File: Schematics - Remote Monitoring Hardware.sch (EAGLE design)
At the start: 49 parts, among them IC1 MSP430G2 Socket, IC2 TPS77301, IC3 Xbee S3 Socket, IC4 MAX31855T, J7 53047-06, Q1 MC-405

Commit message: board and schematics update May 25 2017
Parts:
- removed J5: (no value), SparkFun-Connectors:CONN_023.5MM
- added J5A: (no value), SparkFun-Connectors:CONN_023.5MM
- added J5B: PCC-SMP, custom parts:PCC-SMP
- C7: value 1uF/6.3V -> 10uF
- C8: value 100uF -> 100nF
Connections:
- removed net DIN: J6.2
- removed net DOUT: J6.3
- net N$14: now also J5A.2, J5B.T-; no longer J5.2
- net N$15: now also J5A.1, J5B.T+; no longer J5.1
- net P1.1: now also J6.3
- net P1.2: now also J6.2
- net VCC: now also S2.1; no longer S2.2
- net VCC_XBEE: now also S2.2; no longer S2.1
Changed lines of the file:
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@@
 <classes>
 <class number="0" name="default" width="0.2032" drill="0">
+<clearance class="0" value="0.205"/>
 </class>
 <class number="1" name="vcc" width="0.3048" drill="0">
@@
 <part name="C6" library="eagle-ltspice" deviceset="C" device="" value="100nF"/>
 <part name="IC2" library="texas" deviceset="TPS773*" device="" technology="01"/>
-<part name="C7" library="eagle-ltspice" deviceset="C" device="" value="1uF/6.3V"/>
+<part name="C7" library="eagle-ltspice" deviceset="C" device="" value="10uF"/>
 <part name="GND7" library="supply1" deviceset="GND" device=""/>
 <part name="R5" library="eagle-ltspice" deviceset="R" device="" value="53.8k"/>
@@
 <part name="GND9" library="supply1" deviceset="GND" device=""/>
 <part name="R7" library="eagle-ltspice" deviceset="R" device="" value="250k"/>
-<part name="C8" library="eagle-ltspice" deviceset="C" device="" value="100uF"/>
+<part name="C8" library="eagle-ltspice" deviceset="C" device="" value="100nF"/>
 <part name="GND10" library="supply1" deviceset="GND" device=""/>
 <part name="GND11" library="supply1" deviceset="GND" device=""/>
@@
 <part name="J4" library="SparkFun-Connectors" deviceset="CONN_02" device="3.5MM"/>
 <part name="Q1" library="crystal" deviceset="MC-405" device=""/>
-<part name="J5" library="SparkFun-Connectors" deviceset="CONN_02" device="3.5MM"/>
+<part name="J5A" library="SparkFun-Connectors" deviceset="CONN_02" device="3.5MM"/>
+<part name="J5B" library="custom parts" deviceset="PCC-SMP" device=""/>
 </parts>
 <sheets>
@@
 </instance>
 <instance part="Q1" gate="P" x="38.1" y="55.88" rot="R90"/>
-<instance part="J5" gate="G$1" x="27.94" y="109.22" smashed="yes">
-<attribute name="VALUE" x="22.86" y="104.394" size="1.778" layer="96" font="vector"/>
-<attribute name="NAME" x="25.4" y="114.808" size="1.778" layer="95" font="vector"/>
+<instance part="J5A" gate="G$1" x="27.94" y="114.3" smashed="yes">
+<attribute name="VALUE" x="22.86" y="109.474" size="1.778" layer="96" font="vector"/>
+<attribute name="NAME" x="25.4" y="119.888" size="1.778" layer="95" font="vector"/>
 </instance>
+<instance part="J5B" gate="G$1" x="25.4" y="106.68"/>
 </instances>
 <busses>
@@
 <label x="228.6" y="58.42" size="1.778" layer="95"/>
 <pinref part="J7" gate="-5" pin="S"/>
-</segment>
-<segment>
-<pinref part="S2" gate="G$1" pin="2"/>
-<wire x1="187.96" y1="198.12" x2="195.58" y2="198.12" width="0.1524" layer="91"/>
-<label x="193.04" y="198.12" size="1.778" layer="95"/>
 </segment>
 <segment>
@@
 <label x="63.5" y="134.62" size="1.778" layer="95"/>
 </segment>
+<segment>
+<pinref part="S2" gate="G$1" pin="1"/>
+<wire x1="187.96" y1="195.58" x2="195.58" y2="195.58" width="0.1524" layer="91"/>
+<label x="193.04" y="195.58" size="1.778" layer="95"/>
+</segment>
 </net>
 <net name="P1.0" class="0">
@@
 <label x="228.6" y="48.26" size="1.778" layer="95"/>
 <pinref part="J7" gate="-1" pin="S"/>
+</segment>
+<segment>
+<pinref part="J6" gate="1" pin="2"/>
+<wire x1="185.42" y1="53.34" x2="195.58" y2="53.34" width="0.1524" layer="91"/>
+<label x="190.5" y="53.34" size="1.778" layer="95"/>
 </segment>
 </net>
@@
 <label x="228.6" y="60.96" size="1.778" layer="95"/>
 <pinref part="J7" gate="-6" pin="S"/>
+</segment>
+<segment>
+<pinref part="J6" gate="1" pin="3"/>
+<wire x1="185.42" y1="55.88" x2="195.58" y2="55.88" width="0.1524" layer="91"/>
+<label x="190.5" y="55.88" size="1.778" layer="95"/>
 </segment>
 </net>
@@
 <net name="N$14" class="0">
 <segment>
-<wire x1="38.1" y1="111.76" x2="38.1" y2="116.84" width="0.1524" layer="91"/>
 <pinref part="L1" gate="G$1" pin="2"/>
+<wire x1="35.56" y1="116.84" x2="38.1" y2="116.84" width="0.1524" layer="91"/>
+<pinref part="J5A" gate="G$1" pin="2"/>
 <wire x1="38.1" y1="116.84" x2="43.18" y2="116.84" width="0.1524" layer="91"/>
-<wire x1="38.1" y1="111.76" x2="35.56" y2="111.76" width="0.1524" layer="91"/>
-<pinref part="J5" gate="G$1" pin="2"/>
+<wire x1="33.02" y1="109.22" x2="38.1" y2="109.22" width="0.1524" layer="91"/>
+<wire x1="38.1" y1="109.22" x2="38.1" y2="116.84" width="0.1524" layer="91"/>
+<junction x="38.1" y="116.84"/>
+<pinref part="J5B" gate="G$1" pin="T-"/>
 </segment>
 </net>
 <net name="N$15" class="0">
 <segment>
-<wire x1="38.1" y1="109.22" x2="38.1" y2="104.14" width="0.1524" layer="91"/>
 <pinref part="L2" gate="G$1" pin="1"/>
-<wire x1="38.1" y1="104.14" x2="43.18" y2="104.14" width="0.1524" layer="91"/>
-<wire x1="35.56" y1="109.22" x2="38.1" y2="109.22" width="0.1524" layer="91"/>
-<pinref part="J5" gate="G$1" pin="1"/>
+<pinref part="J5A" gate="G$1" pin="1"/>
+<wire x1="40.64" y1="104.14" x2="43.18" y2="104.14" width="0.1524" layer="91"/>
+<wire x1="35.56" y1="114.3" x2="40.64" y2="114.3" width="0.1524" layer="91"/>
+<wire x1="40.64" y1="114.3" x2="40.64" y2="104.14" width="0.1524" layer="91"/>
+<junction x="40.64" y="104.14"/>
+<wire x1="33.02" y1="104.14" x2="40.64" y2="104.14" width="0.1524" layer="91"/>
+<pinref part="J5B" gate="G$1" pin="T+"/>
 </segment>
 </net>
@@
 </segment>
 <segment>
-<pinref part="S2" gate="G$1" pin="1"/>
-<wire x1="187.96" y1="195.58" x2="195.58" y2="195.58" width="0.1524" layer="91"/>
-<label x="193.04" y="195.58" size="1.778" layer="95"/>
-</segment>
-<segment>
 <wire x1="218.44" y1="109.22" x2="218.44" y2="106.68" width="0.1524" layer="91"/>
 <pinref part="R14" gate="G$1" pin="2"/>
@@
 <label x="190.5" y="50.8" size="1.778" layer="95"/>
 </segment>
+<segment>
+<pinref part="S2" gate="G$1" pin="2"/>
+<wire x1="187.96" y1="198.12" x2="195.58" y2="198.12" width="0.1524" layer="91"/>
+<label x="193.04" y="198.12" size="1.778" layer="95"/>
+</segment>
 </net>
 <net name="N$17" class="0">
@@
 </segment>
 </net>
-<net name="DOUT" class="0">
-<segment>
-<pinref part="J6" gate="1" pin="3"/>
-<wire x1="185.42" y1="55.88" x2="195.58" y2="55.88" width="0.1524" layer="91"/>
-<label x="190.5" y="55.88" size="1.778" layer="95"/>
-</segment>
-</net>
-<net name="DIN" class="0">
-<segment>
-<pinref part="J6" gate="1" pin="2"/>
-<wire x1="185.42" y1="53.34" x2="195.58" y2="53.34" width="0.1524" layer="91"/>
-<label x="190.5" y="53.34" size="1.778" layer="95"/>
-</segment>
-</net>

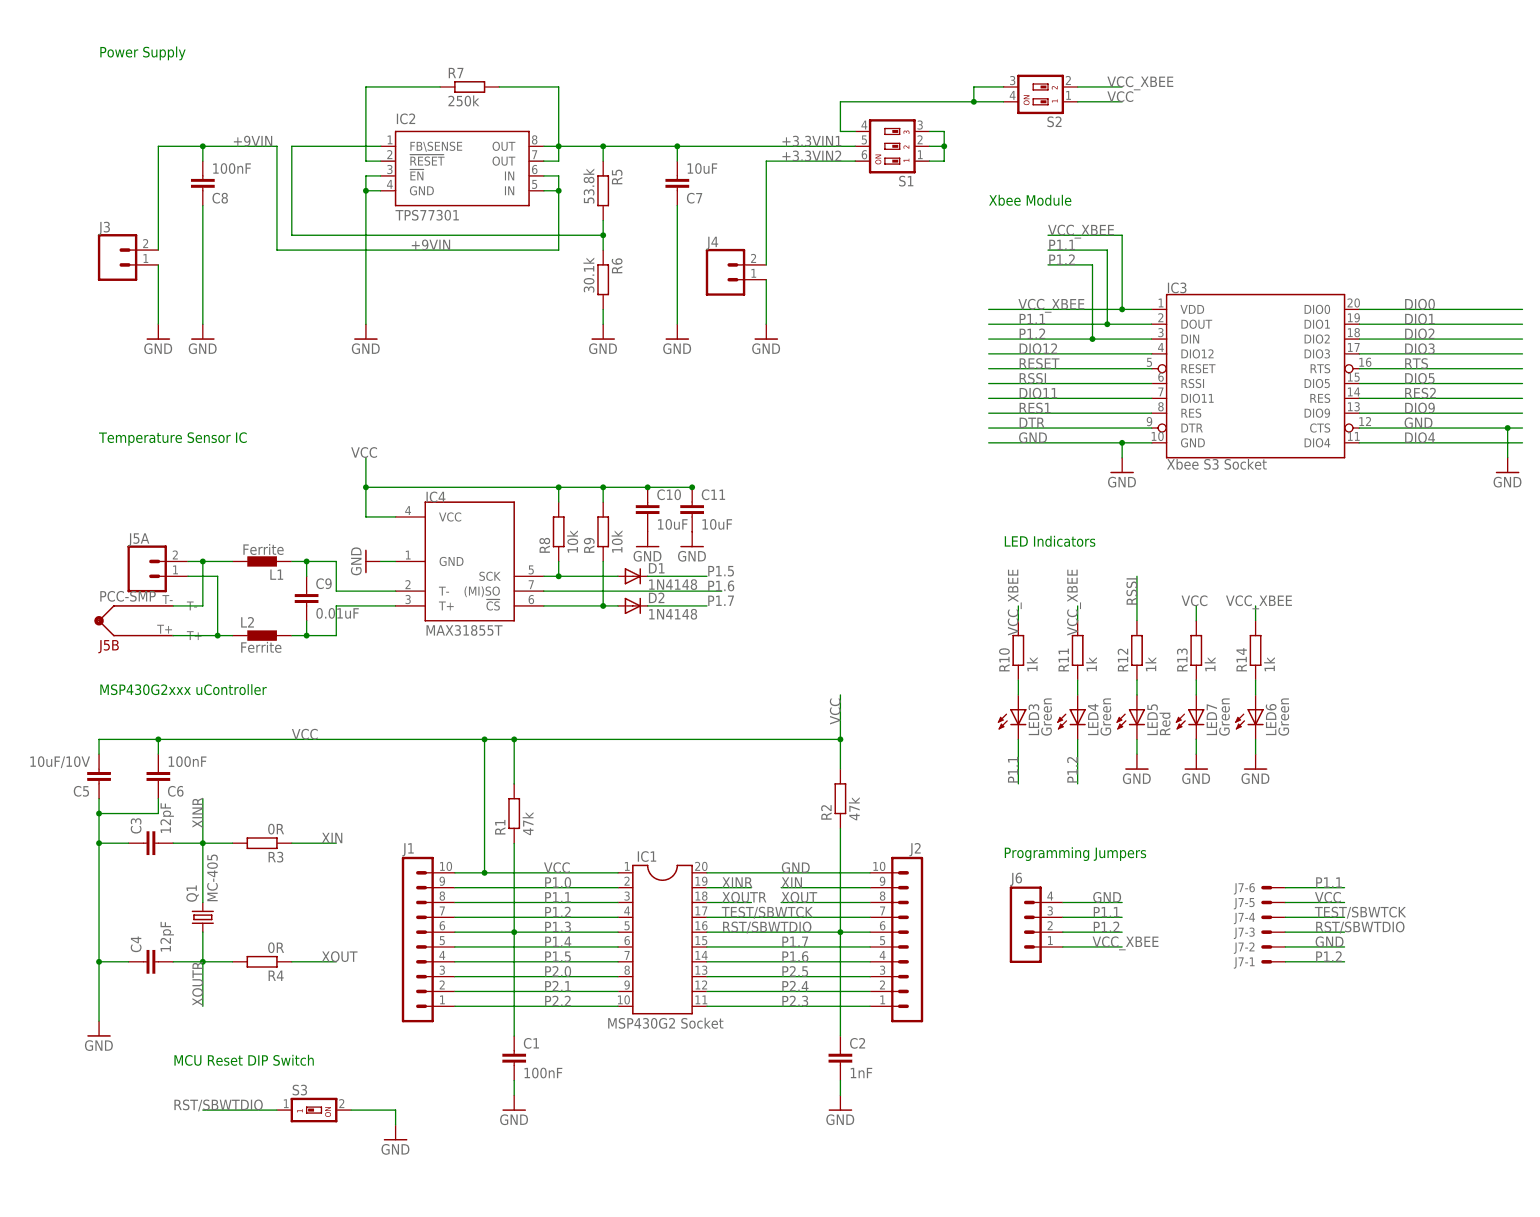
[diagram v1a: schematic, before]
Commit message: Added BOM + brd & sch changes Aug 28 2017
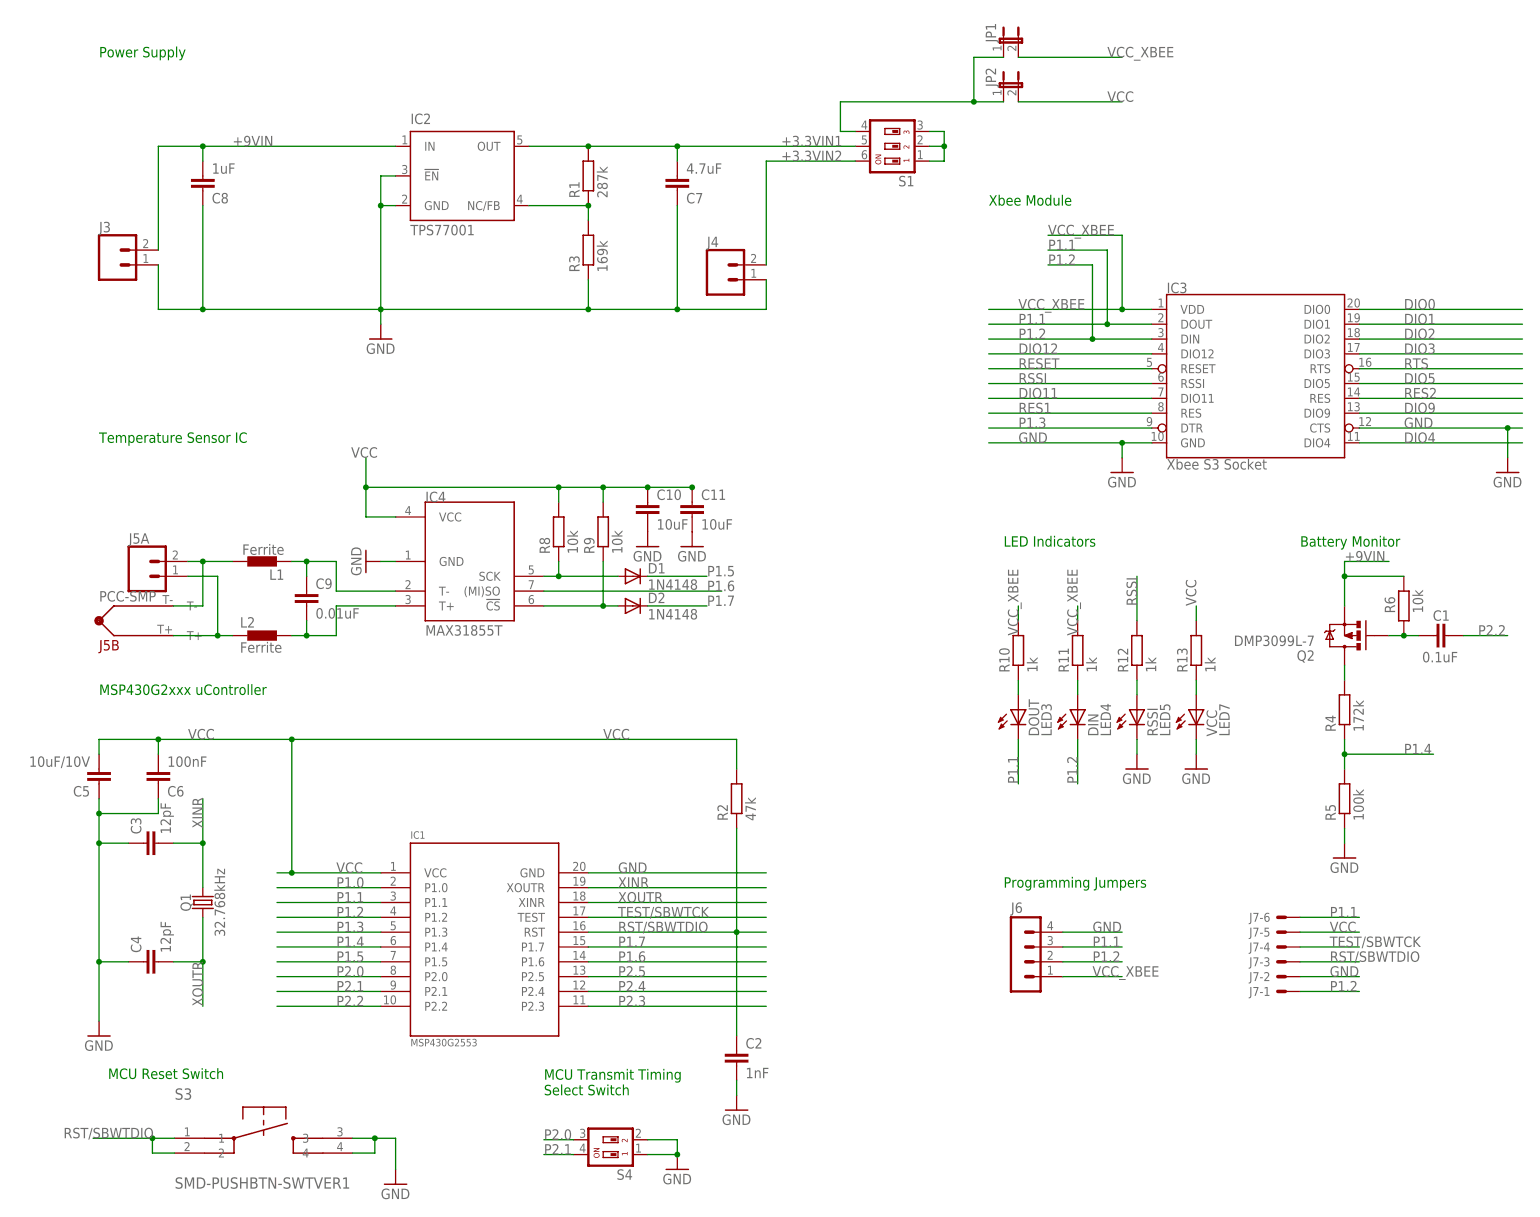
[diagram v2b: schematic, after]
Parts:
- removed J1, J2: (no value), con-lstb:MA10-1
- removed LED3, LED4, LED6, LED7: Green, eagle-ltspice:LED_E
- removed LED5: Red, eagle-ltspice:LED_E
- removed R14: 1k, eagle-ltspice:R
- removed R7: 250k, eagle-ltspice:R
- removed S2: SWS002, smd-special:SWS002
- added DIN: LED4, led:LEDSML0805
- added DOUT: LED3, led:LEDSML0805
- added JP1, JP2: (no value), SparkFun-Retired:JUMPER-2PTH
- added Q2: DMP3099L-7, User-Submitted:MOSFET-PCHANNELIRLML2244
- added RSSI: LED5, led:LEDSML0805
- added S4: SWS002, smd-special:SWS002
- added VCC: LED7, led:LEDSML0805
- C1: value 100nF -> 0.1uF
- C7: value 10uF -> 4.7uF
- C8: value 100nF -> 1uF
- IC1: value MSP430G2 Socket -> MSP430G2553; device ic-package:DIL20S -> custom parts:MSP430G2553IPW20VER2TSSOP-20
- IC2: value TPS77301 -> TPS77001; device texas:TPS77301 -> texas:TPS77001
- Q1: value MC-405 -> 32.768kHz; device crystal:MC-405 -> SparkFun-Clocks:CRYSTAL-32.768KHZSMD-2X6
- R1: value 47k -> 287k
- R3: value 0R -> 169k
- R4: value 0R -> 172k
- R5: value 53.8k -> 100k
- R6: value 30.1k -> 10k
- S3: value SWS001 -> SMD-PUSHBTN-SWTVER1; device smd-special:SWS001 -> custom parts:SMD-PUSHBTN-SWTVER1
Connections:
- removed net DTR: IC3.DTR
- removed net N$18: LED6.A, R14.1
- removed net XIN: J2.9, R3.1
- removed net XOUT: J2.8, R4.1
- new net N$3: Q2.D, R4.2
- net +3.3VIN1: now also IC2.OUT, R1.2; no longer IC2.OUT@1, IC2.OUT@2, R5.1, R7.2
- net +9VIN: now also IC2.IN, Q2.S, R6.2; no longer IC2.IN@1, IC2.IN@2
- net GND: now also IC1.GND, R3.1, R5.1, RSSI.C, S3.3, S3.4, S4.1, S4.2, VCC.C; no longer C1.2, IC1.20, J2.10, LED5.C, LED6.C, LED7.C, R6.2, S3.2
- net N$10: now also DIN.A; no longer LED4.A
- net N$11: now also RSSI.A; no longer LED5.A
- net N$16: now also JP1.1, JP2.1; no longer S2.3, S2.4
- net N$17: now also VCC.A; no longer LED7.A
- net N$2: now also C1.2, Q2.G; no longer IC2.FB\SENSE, R5.2
- net N$4: now also DOUT.A; no longer LED3.A
- net N$5: now also IC2.NC/FB, R1.1, R3.2; no longer IC2.!RESET, R7.1
- net P1.0: now also IC1.P1.0; no longer IC1.2, J1.9
- net P1.1: now also DOUT.C, IC1.P1.1; no longer IC1.3, J1.8, LED3.C
- net P1.2: now also DIN.C, IC1.P1.2; no longer IC1.4, J1.7, LED4.C
- net P1.3: now also IC1.P1.3, IC3.DTR; no longer C1.1, IC1.5, J1.6, R1.1
- net P1.4: now also IC1.P1.4, R4.1, R5.2; no longer IC1.6, J1.5
- net P1.5: now also IC1.P1.5; no longer IC1.7, J1.4
- net P1.6: now also IC1.P1.6; no longer IC1.14, J2.4
- net P1.7: now also IC1.P1.7; no longer IC1.15, J2.5
- net P2.0: now also IC1.P2.0, S4.3; no longer IC1.8, J1.3
- net P2.1: now also IC1.P2.1, S4.4; no longer IC1.9, J1.2
- net P2.2: now also C1.1, IC1.P2.2; no longer IC1.10, J1.1
- net P2.3: now also IC1.P2.3; no longer IC1.11, J2.1
- net P2.4: now also IC1.P2.4; no longer IC1.12, J2.2
- net P2.5: now also IC1.P2.5; no longer IC1.13, J2.3
- net RST/SBWTDIO: now also IC1.RST, S3.2; no longer IC1.16, J2.6
- net TEST/SBWTCK: now also IC1.TEST; no longer IC1.17, J2.7
- net VCC: now also IC1.VCC, JP2.2; no longer IC1.1, J1.10, R1.2, S2.1
- net VCC_XBEE: now also JP1.2; no longer R14.2, S2.2
- net XINR: now also IC1.XOUTR; no longer IC1.19, R3.2
- net XOUTR: now also IC1.XINR; no longer IC1.18, R4.2
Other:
- note added: "Battery Monitor"
- note added: "MCU Reset Switch"
- note added: "MCU Transmit Timing Select Switch"
- note removed: "MCU Reset DIP Switch"
- moved on the sheet: C1, C2, J6, J7-1, J7-2, J7-3, J7-4, J7-5, J7-6, R1, R2, R3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
